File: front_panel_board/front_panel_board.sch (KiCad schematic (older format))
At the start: 10 parts, among them J1 Molex_SL_01x02_Male, J2 Conn_02x05_Odd_Even, J3 Conn_02x05_Odd_Even, J4 Molex_SL_01x02_Male, SW1 SW_Rotary8_CK_A125xxxxCxx, SW2 SW_SPDT

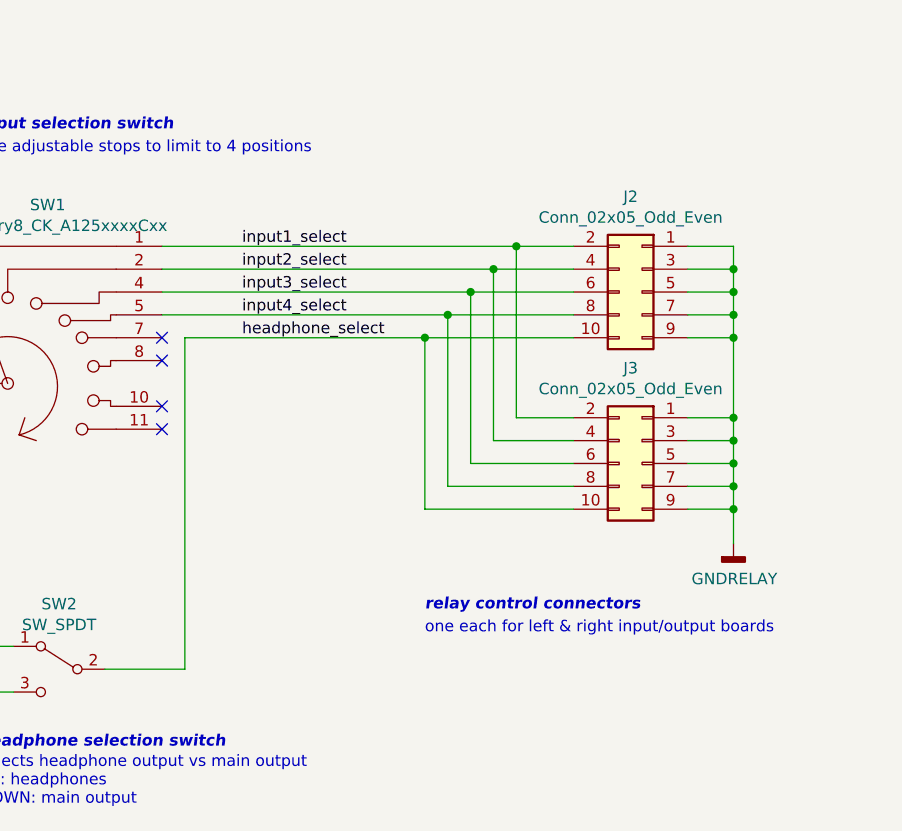
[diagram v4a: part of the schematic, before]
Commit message: update relay connector pin numbering. redo a lot of layout. update silk (rev1)
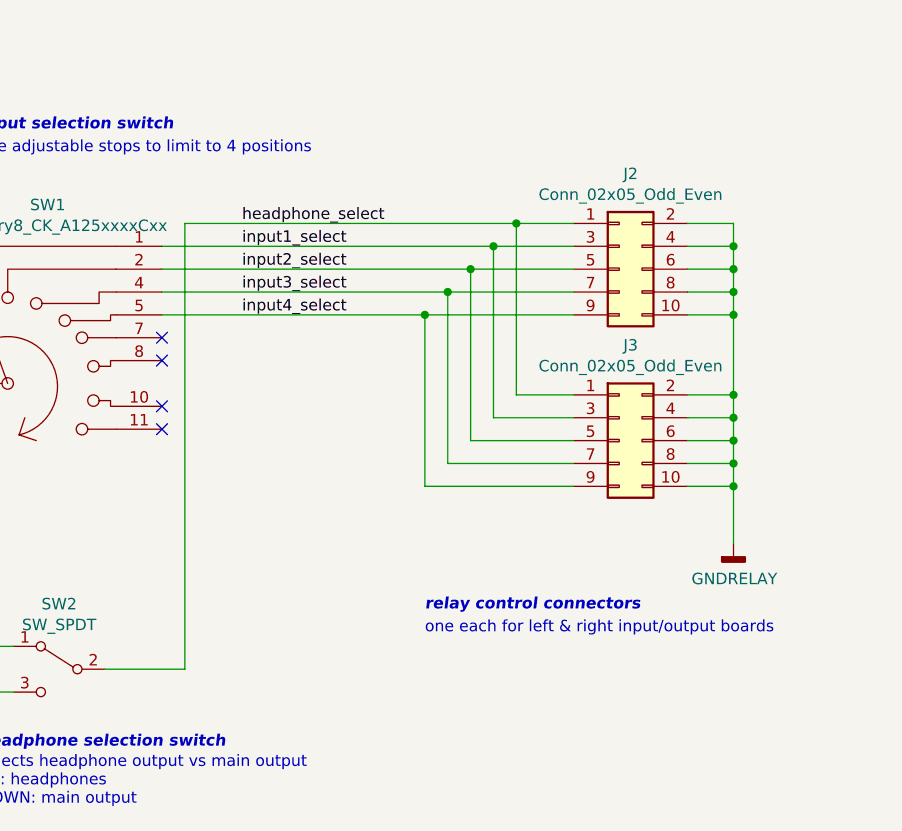
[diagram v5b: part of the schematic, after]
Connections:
- net GNDRELAY: now also J2.10 (Pin_10), J2.2 (Pin_2), J2.4 (Pin_4), J2.6 (Pin_6), J2.8 (Pin_8), J3.10 (Pin_10), J3.2 (Pin_2), J3.4 (Pin_4), J3.6 (Pin_6), J3.8 (Pin_8); no longer J2.1 (Pin_1), J2.3 (Pin_3), J2.5 (Pin_5), J2.7 (Pin_7), J2.9 (Pin_9), J3.1 (Pin_1), J3.3 (Pin_3), J3.5 (Pin_5), J3.7 (Pin_7), J3.9 (Pin_9)
- net headphone_select: now also J2.1 (Pin_1), J3.1 (Pin_1); no longer J2.10 (Pin_10), J3.10 (Pin_10)
- net input1_select: now also J2.3 (Pin_3), J3.3 (Pin_3); no longer J2.2 (Pin_2), J3.2 (Pin_2)
- net input2_select: now also J2.5 (Pin_5), J3.5 (Pin_5); no longer J2.4 (Pin_4), J3.4 (Pin_4)
- net input3_select: now also J2.7 (Pin_7), J3.7 (Pin_7); no longer J2.6 (Pin_6), J3.6 (Pin_6)
- net input4_select: now also J2.9 (Pin_9), J3.9 (Pin_9); no longer J2.8 (Pin_8), J3.8 (Pin_8)
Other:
- moved on the sheet: J2, J3
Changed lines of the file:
@@
 EESchema Schematic File Version 4
-LIBS:front_panel_board-cache
 EELAYER 30 0
 EELAYER END
@@
 NoConn ~ 5000 3800
 Wire Wire Line
-	5100 3400 5100 4850
+	5100 2900 5100 4850
 Text Notes 4200 2600 0    50   ~ 0
 use adjustable stops to limit to 4 positions
@@
 	1    0    0    -1
 $EndComp
-Text Label 5350 3400 0    50   ~ 0
+Text Label 5350 2900 0    50   ~ 0
 headphone_select
 Text Label 5350 3300 0    50   ~ 0
@@
 Text Label 5350 3000 0    50   ~ 0
 input1_select
-Connection ~ 6150 3400
-Wire Wire Line
-	5100 3400 6150 3400
-Wire Wire Line
-	6150 3400 6150 4150
-Wire Wire Line
-	6250 3300 5000 3300
-Connection ~ 6250 3300
-Wire Wire Line
-	6250 3300 6250 4050
-Connection ~ 6350 3200
-Wire Wire Line
-	5000 3200 6350 3200
-Wire Wire Line
-	6350 3200 6350 3950
-Wire Wire Line
-	6450 3100 5000 3100
-Connection ~ 6450 3100
-Wire Wire Line
-	6450 3100 6450 3850
-Wire Wire Line
-	5000 3000 6550 3000
-Connection ~ 6550 3000
-Wire Wire Line
-	6550 3750 6550 3000
-Wire Wire Line
-	7500 4150 7500 4050
-Connection ~ 7500 4150
-Wire Wire Line
-	7300 4150 7500 4150
+Connection ~ 6550 2900
+Wire Wire Line
+	5100 2900 6550 2900
+Wire Wire Line
+	6550 2900 6550 3650
+Wire Wire Line
+	6150 3300 5000 3300
+Connection ~ 6150 3300
+Wire Wire Line
+	6150 3300 6150 4050
+Connection ~ 6250 3200
+Wire Wire Line
+	5000 3200 6250 3200
+Wire Wire Line
+	6250 3200 6250 3950
+Wire Wire Line
+	6350 3100 5000 3100
+Connection ~ 6350 3100
+Wire Wire Line
+	6350 3100 6350 3850
+Wire Wire Line
+	5000 3000 6450 3000
+Connection ~ 6450 3000
+Wire Wire Line
+	6450 3750 6450 3000
 Wire Wire Line
 	7500 4050 7500 3950
 Connection ~ 7500 4050
 Wire Wire Line
-	7300 4050 7500 4050
-Wire Wire Line
 	7500 3950 7500 3850
 Connection ~ 7500 3950
 Wire Wire Line
-	7300 3950 7500 3950
-Wire Wire Line
 	7500 3850 7500 3750
 Connection ~ 7500 3850
-Wire Wire Line
-	7500 3850 7300 3850
-Wire Wire Line
-	7500 3750 7500 3400
 Connection ~ 7500 3750
-Wire Wire Line
-	7300 3750 7500 3750
-Wire Wire Line
-	7500 3400 7500 3300
-Connection ~ 7500 3400
-Wire Wire Line
-	7300 3400 7500 3400
 Wire Wire Line
 	7500 3300 7500 3200
 Connection ~ 7500 3300
 Wire Wire Line
-	7300 3300 7500 3300
-Wire Wire Line
 	7500 3200 7500 3100
 Connection ~ 7500 3200
 Wire Wire Line
-	7300 3200 7500 3200
-Wire Wire Line
 	7500 3100 7500 3000
 Connection ~ 7500 3100
-Wire Wire Line
-	7300 3100 7500 3100
-Wire Wire Line
-	7500 3000 7300 3000
-Wire Wire Line
-	7500 4300 7500 4150
 $Comp
 L power_gkeeth:GNDRELAY #PWR0105
@@
 $EndComp
 Wire Wire Line
-	6250 4050 6800 4050
-Wire Wire Line
-	6350 3950 6800 3950
-Wire Wire Line
-	6450 3850 6800 3850
-Wire Wire Line
-	6800 3750 6550 3750
-Wire Wire Line
-	6150 4150 6800 4150
+	6150 4050 6800 4050
+Wire Wire Line
+	6250 3950 6800 3950
+Wire Wire Line
+	6350 3850 6800 3850
+Wire Wire Line
+	6800 3750 6450 3750
+Wire Wire Line
+	6550 3650 6800 3650
 $Comp
 L Connector_Generic:Conn_02x05_Odd_Even J3
 U 1 1 5D106F42
-P 7100 3950
-F 0 "J3" H 7150 4367 50  0000 C CNN
-F 1 "Conn_02x05_Odd_Even" H 7150 4276 50  0000 C CNN
-F 2 "Connector_Molex_C-Grid:Molex_C-Grid_70246-1001_2x05_P2.54mm_Vertical" H 7100 3950 50  0001 C CNN
-F 3 "https://www.molex.com/pdm_docs/sd/702461001_sd.pdf" H 7100 3950 50  0001 C CNN
-F 4 "Digikey" H 7100 3950 50  0001 C CNN "Distributor"
-F 5 "WM9219-ND" H 7100 3950 50  0001 C CNN "Distributor PN"
-F 6 "Molex" H 7100 3950 50  0001 C CNN "Manufacturer"
-F 7 "0702461001" H 7100 3950 50  0001 C CNN "Manufacturer PN"
-F 8 "https://www.digikey.com/products/en?keywords=70246-1001" H 7100 3950 50  0001 C CNN "URL"
-F 9 "1.70" H 7100 3950 50  0001 C CNN "Unit Price"
-	1    7100 3950
-	-1   0    0    -1
-$EndComp
-Wire Wire Line
-	6800 3300 6250 3300
-Wire Wire Line
-	6350 3200 6800 3200
-Wire Wire Line
-	6800 3100 6450 3100
-Wire Wire Line
-	6550 3000 6800 3000
-Wire Wire Line
-	6150 3400 6800 3400
+P 7000 3850
+F 0 "J3" H 7050 4267 50  0000 C CNN
+F 1 "Conn_02x05_Odd_Even" H 7050 4176 50  0000 C CNN
+F 2 "Connector_Molex_C-Grid:Molex_C-Grid_70246-1001_2x05_P2.54mm_Vertical" H 7000 3850 50  0001 C CNN
+F 3 "https://www.molex.com/pdm_docs/sd/702461001_sd.pdf" H 7000 3850 50  0001 C CNN
+F 4 "Digikey" H 7000 3850 50  0001 C CNN "Distributor"
+F 5 "WM9219-ND" H 7000 3850 50  0001 C CNN "Distributor PN"
+F 6 "Molex" H 7000 3850 50  0001 C CNN "Manufacturer"
+F 7 "0702461001" H 7000 3850 50  0001 C CNN "Manufacturer PN"
+F 8 "https://www.digikey.com/products/en?keywords=70246-1001" H 7000 3850 50  0001 C CNN "URL"
+F 9 "1.70" H 7000 3850 50  0001 C CNN "Unit Price"
+	1    7000 3850
+	1    0    0    -1
+$EndComp
+Wire Wire Line
+	6800 3300 6150 3300
+Wire Wire Line
+	6250 3200 6800 3200
+Wire Wire Line
+	6800 3100 6350 3100
+Wire Wire Line
+	6450 3000 6800 3000
+Wire Wire Line
+	6550 2900 6800 2900
 $Comp
 L Connector_Generic:Conn_02x05_Odd_Even J2
 U 1 1 5CD2571D
-P 7100 3200
-F 0 "J2" H 7150 3617 50  0000 C CNN
-F 1 "Conn_02x05_Odd_Even" H 7150 3526 50  0000 C CNN
-F 2 "Connector_Molex_C-Grid:Molex_C-Grid_70246-1001_2x05_P2.54mm_Vertical" H 7100 3200 50  0001 C CNN
-F 3 "https://www.molex.com/pdm_docs/sd/702461001_sd.pdf" H 7100 3200 50  0001 C CNN
-F 4 "Digikey" H 7100 3200 50  0001 C CNN "Distributor"
-F 5 "WM9219-ND" H 7100 3200 50  0001 C CNN "Distributor PN"
-F 6 "Molex" H 7100 3200 50  0001 C CNN "Manufacturer"
-F 7 "0702461001" H 7100 3200 50  0001 C CNN "Manufacturer PN"
-F 8 "https://www.digikey.com/products/en?keywords=70246-1001" H 7100 3200 50  0001 C CNN "URL"
-F 9 "1.70" H 7100 3200 50  0001 C CNN "Unit Price"
-	1    7100 3200
-	-1   0    0    -1
+P 7000 3100
+F 0 "J2" H 7050 3517 50  0000 C CNN
+F 1 "Conn_02x05_Odd_Even" H 7050 3426 50  0000 C CNN
+F 2 "Connector_Molex_C-Grid:Molex_C-Grid_70246-1001_2x05_P2.54mm_Vertical" H 7000 3100 50  0001 C CNN
+F 3 "https://www.molex.com/pdm_docs/sd/702461001_sd.pdf" H 7000 3100 50  0001 C CNN
+F 4 "Digikey" H 7000 3100 50  0001 C CNN "Distributor"
+F 5 "WM9219-ND" H 7000 3100 50  0001 C CNN "Distributor PN"
+F 6 "Molex" H 7000 3100 50  0001 C CNN "Manufacturer"
+F 7 "0702461001" H 7000 3100 50  0001 C CNN "Manufacturer PN"
+F 8 "https://www.digikey.com/products/en?keywords=70246-1001" H 7000 3100 50  0001 C CNN "URL"
+F 9 "1.70" H 7000 3100 50  0001 C CNN "Unit Price"
+	1    7000 3100
+	1    0    0    -1
 $EndComp
 $Comp
@@
 	1    0    0    -1
 $EndComp
+Wire Wire Line
+	7300 4050 7500 4050
+Wire Wire Line
+	7300 3950 7500 3950
+Wire Wire Line
+	7300 3850 7500 3850
+Wire Wire Line
+	7300 3750 7500 3750
+Wire Wire Line
+	7300 3300 7500 3300
+Wire Wire Line
+	7300 3200 7500 3200
+Wire Wire Line
+	7300 3100 7500 3100
+Wire Wire Line
+	7300 3000 7500 3000
+Wire Wire Line
+	7500 3300 7500 3650
+Wire Wire Line
+	7500 4050 7500 4300
+Wire Wire Line
+	7300 3650 7500 3650
+Connection ~ 7500 3650
+Wire Wire Line
+	7500 3650 7500 3750
+Wire Wire Line
+	7300 2900 7500 2900
+Wire Wire Line
+	7500 2900 7500 3000
+Connection ~ 7500 3000
 $EndSCHEMATC
